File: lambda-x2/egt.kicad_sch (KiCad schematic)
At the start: 17 parts, among them U1 MAX31855KASA, U15 MAX31856

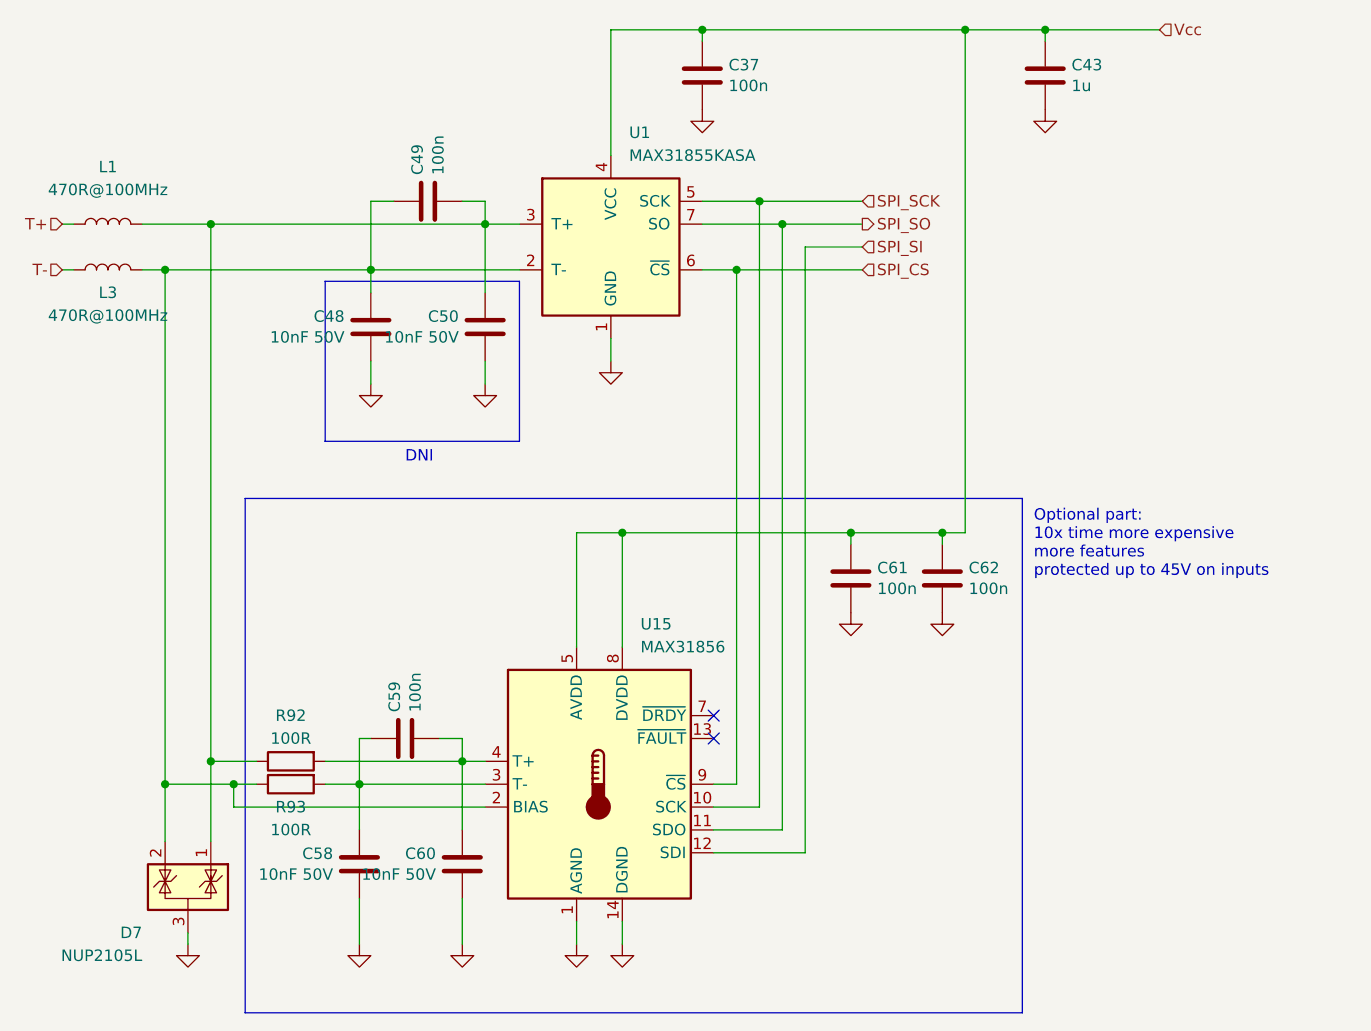
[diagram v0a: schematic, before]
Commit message: First version for lambda-x2 based on rev1
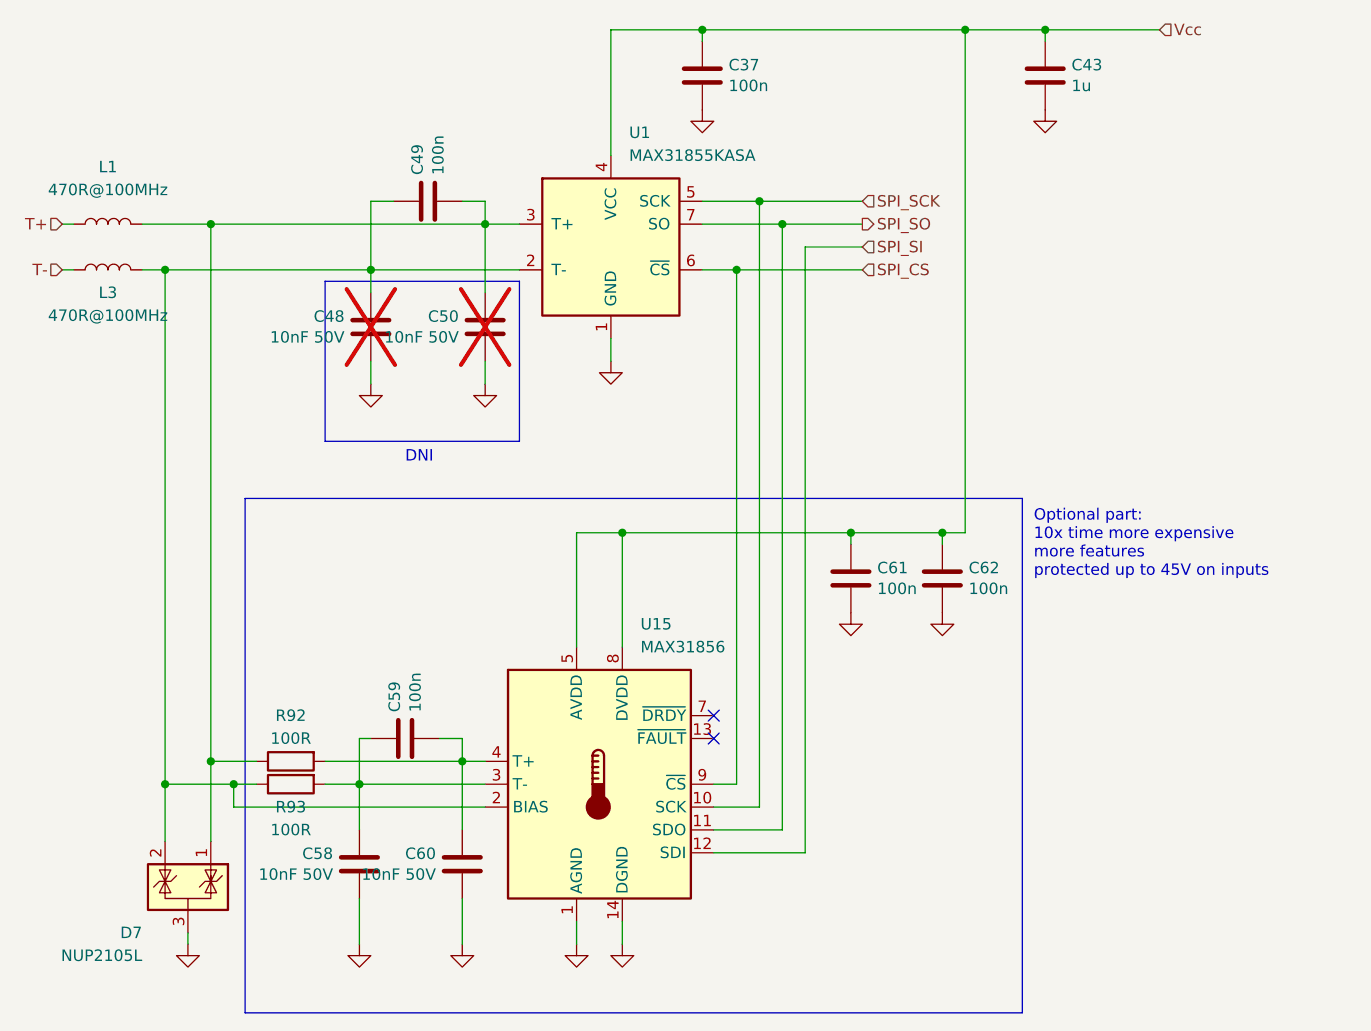
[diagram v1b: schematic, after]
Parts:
- C48, C50: now not fitted

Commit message: Further updates for Rev2
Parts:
- removed D7: NUP2105L, Package_TO_SOT_SMD:SOT-23, symbol Power_Protection:NUP2105L
- C58, C60, U15: now not fitted
- C59, C61, C62: now not fitted; now left out of the parts list
- L1, L3: value 470R@100MHz -> 600R@100MHz; LCSC C97853 -> C1002
- R92, R93: LCSC C106233 -> C25076; now not fitted; now left out of the parts list
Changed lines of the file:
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@@
   (junction (at 93.98 46.99) (diameter 0) (color 0 0 0 0)
   )
-  (junction (at 30.48 104.14) (diameter 0) (color 0 0 0 0)
-  )
   (junction (at 66.04 41.91) (diameter 0) (color 0 0 0 0)
-  )
-  (junction (at 35.56 101.6) (diameter 0) (color 0 0 0 0)
   )
   (junction (at 35.56 41.91) (diameter 0) (color 0 0 0 0)
@@
     (stroke (width 0) (type default))
   )
-  (wire (pts (xy 33.02 121.92) (xy 33.02 120.65))
-    (stroke (width 0) (type default))
-  )
   (wire (pts (xy 99.06 109.22) (xy 99.06 41.91))
     (stroke (width 0) (type default))
@@
     (stroke (width 0) (type default))
   )
-  (wire (pts (xy 35.56 101.6) (xy 35.56 110.49))
-    (stroke (width 0) (type default))
-  )
   (wire (pts (xy 53.34 57.15) (xy 53.34 59.69))
     (stroke (width 0) (type default))
@@
   )
   (wire (pts (xy 53.34 46.99) (xy 53.34 49.53))
-    (stroke (width 0) (type default))
-  )
-  (wire (pts (xy 30.48 104.14) (xy 30.48 110.49))
     (stroke (width 0) (type default))
   )
@@
   )
   (symbol (lib_id "Device:C") (at 57.15 99.06 90) (unit 1)
-    (in_bom yes) (on_board yes) (dnp no)
+    (in_bom no) (on_board yes) (dnp yes)
     (property "Reference" "C59" (at 55.9816 96.139 0)
       (effects (font (size 1.27 1.27)) (justify left))
@@
     )
   )
-  (symbol (lib_id "Power_Protection:NUP2105L") (at 33.02 115.57 0) (mirror y) (unit 1)
-    (in_bom yes) (on_board yes) (dnp no)
-    (property "Reference" "D7" (at 27.94 120.65 0)
-      (effects (font (size 1.27 1.27)) (justify left))
-    )
-    (property "Value" "NUP2105L" (at 27.94 123.19 0)
-      (effects (font (size 1.27 1.27)) (justify left))
-    )
-    (property "Footprint" "Package_TO_SOT_SMD:SOT-23" (at 27.305 116.84 0)
-      (effects (font (size 1.27 1.27)) (justify left) hide)
-    )
-    (property "Datasheet" "http://www.onsemi.com/pub_link/Collateral/NUP2105L-D.PDF" (at 29.845 112.395 0)
-      (effects (font (size 1.27 1.27)) hide)
-    )
-    (property "LCSC" "C284104" (at 33.02 115.57 0)
-      (effects (font (size 1.27 1.27)) hide)
-    )
-    (pin "3")
-    (pin "1")
-    (pin "2")
-    (instances
-      (project "lambda-x2"
-        (path "/3993c707-5291-41b6-83c0-d1c09cb3833a/a9d2c704-8266-40b9-a0a5-1218d3f325f6"
-          (reference "D7") (unit 1)
-        )
-        (path "/3993c707-5291-41b6-83c0-d1c09cb3833a/e339ff66-b3bf-4d0c-a6b6-e4e71fb15e48"
-          (reference "D9") (unit 1)
-        )
-      )
-    )
-  )
   (symbol (lib_id "Device:R") (at 44.45 101.6 90) (mirror x) (unit 1)
-    (in_bom yes) (on_board yes) (dnp no)
+    (in_bom no) (on_board yes) (dnp yes)
     (property "Reference" "R92" (at 44.45 96.52 90)
       (effects (font (size 1.27 1.27)))
@@
       (effects (font (size 1.27 1.27)) hide)
     )
-    (property "LCSC" "C106233" (at 44.45 101.6 90)
+    (property "LCSC" "C25076" (at 44.45 101.6 90)
       (effects (font (size 1.27 1.27)) hide)
     )
@@
   )
   (symbol (lib_id "Device:R") (at 44.45 104.14 90) (mirror x) (unit 1)
-    (in_bom yes) (on_board yes) (dnp no)
+    (in_bom no) (on_board yes) (dnp yes)
     (property "Reference" "R93" (at 44.45 106.68 90)
       (effects (font (size 1.27 1.27)))
@@
       (effects (font (size 1.27 1.27)) hide)
     )
-    (property "LCSC" "C106233" (at 44.45 104.14 90)
+    (property "LCSC" "C25076" (at 44.45 104.14 90)
       (effects (font (size 1.27 1.27)) hide)
     )
@@
   )
   (symbol (lib_id "Device:C") (at 106.68 81.28 0) (unit 1)
-    (in_bom yes) (on_board yes) (dnp no)
+    (in_bom no) (on_board yes) (dnp yes)
     (property "Reference" "C61" (at 109.601 80.1116 0)
       (effects (font (size 1.27 1.27)) (justify left))
@@
       (effects (font (size 1.27 1.27)))
     )
-    (property "Value" "470R@100MHz" (at 24.13 38.1 90)
+    (property "Value" "600R@100MHz" (at 24.13 38.1 90)
       (effects (font (size 1.27 1.27)))
     )
@@
       (effects (font (size 1.27 1.27)) hide)
     )
-    (property "LCSC" "C97853" (at 24.13 41.91 90)
+    (property "LCSC" "C1002" (at 24.13 41.91 90)
       (effects (font (size 1.27 1.27)) hide)
     )
@@
   )
   (symbol (lib_id "Device:C") (at 52.07 113.03 0) (mirror y) (unit 1)
-    (in_bom no) (on_board yes) (dnp no)
+    (in_bom no) (on_board yes) (dnp yes)
     (property "Reference" "C58" (at 49.149 111.8616 0)
       (effects (font (size 1.27 1.27)) (justify left))
@@
       (effects (font (size 1.27 1.27)))
     )
-    (property "Value" "470R@100MHz" (at 24.13 52.07 90)
+    (property "Value" "600R@100MHz" (at 24.13 52.07 90)
       (effects (font (size 1.27 1.27)))
     )
@@
       (effects (font (size 1.27 1.27)) hide)
     )
-    (property "LCSC" "C97853" (at 24.13 46.99 90)
+    (property "LCSC" "C1002" (at 24.13 46.99 90)
       (effects (font (size 1.27 1.27)) hide)
     )
@@
   )
   (symbol (lib_id "Sensor_Temperature:MAX31856") (at 78.74 104.14 0) (unit 1)
-    (in_bom no) (on_board yes) (dnp no) (fields_autoplaced)
+    (in_bom no) (on_board yes) (dnp yes) (fields_autoplaced)
     (property "Reference" "U15" (at 83.2994 86.36 0)
       (effects (font (size 1.27 1.27)) (justify left))
@@
   )
   (symbol (lib_id "Device:C") (at 116.84 81.28 0) (unit 1)
-    (in_bom yes) (on_board yes) (dnp no)
+    (in_bom no) (on_board yes) (dnp yes)
     (property "Reference" "C62" (at 119.761 80.1116 0)
       (effects (font (size 1.27 1.27)) (justify left))
@@
     )
   )
-  (symbol (lib_id "power:GND") (at 33.02 121.92 0) (unit 1)
-    (in_bom yes) (on_board yes) (dnp no)
-    (property "Reference" "#PWR0154" (at 33.02 128.27 0)
-      (effects (font (size 1.27 1.27)) hide)
-    )
-    (property "Value" "GND" (at 33.147 126.3142 0)
-      (effects (font (size 1.27 1.27)) hide)
-    )
-    (property "Footprint" "" (at 33.02 121.92 0)
-      (effects (font (size 1.27 1.27)) hide)
-    )
-    (property "Datasheet" "" (at 33.02 121.92 0)
-      (effects (font (size 1.27 1.27)) hide)
-    )
-    (pin "1")
-    (instances
-      (project "lambda-x2"
-        (path "/3993c707-5291-41b6-83c0-d1c09cb3833a/a9d2c704-8266-40b9-a0a5-1218d3f325f6"
-          (reference "#PWR0154") (unit 1)
-        )
-        (path "/3993c707-5291-41b6-83c0-d1c09cb3833a/e339ff66-b3bf-4d0c-a6b6-e4e71fb15e48"
-          (reference "#PWR0155") (unit 1)
-        )
-      )
-    )
-  )
   (symbol (lib_id "Device:C") (at 63.5 113.03 0) (mirror y) (unit 1)
-    (in_bom no) (on_board yes) (dnp no)
+    (in_bom no) (on_board yes) (dnp yes)
     (property "Reference" "C60" (at 60.579 111.8616 0)
       (effects (font (size 1.27 1.27)) (justify left))
